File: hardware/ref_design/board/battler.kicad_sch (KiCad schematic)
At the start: 9 parts

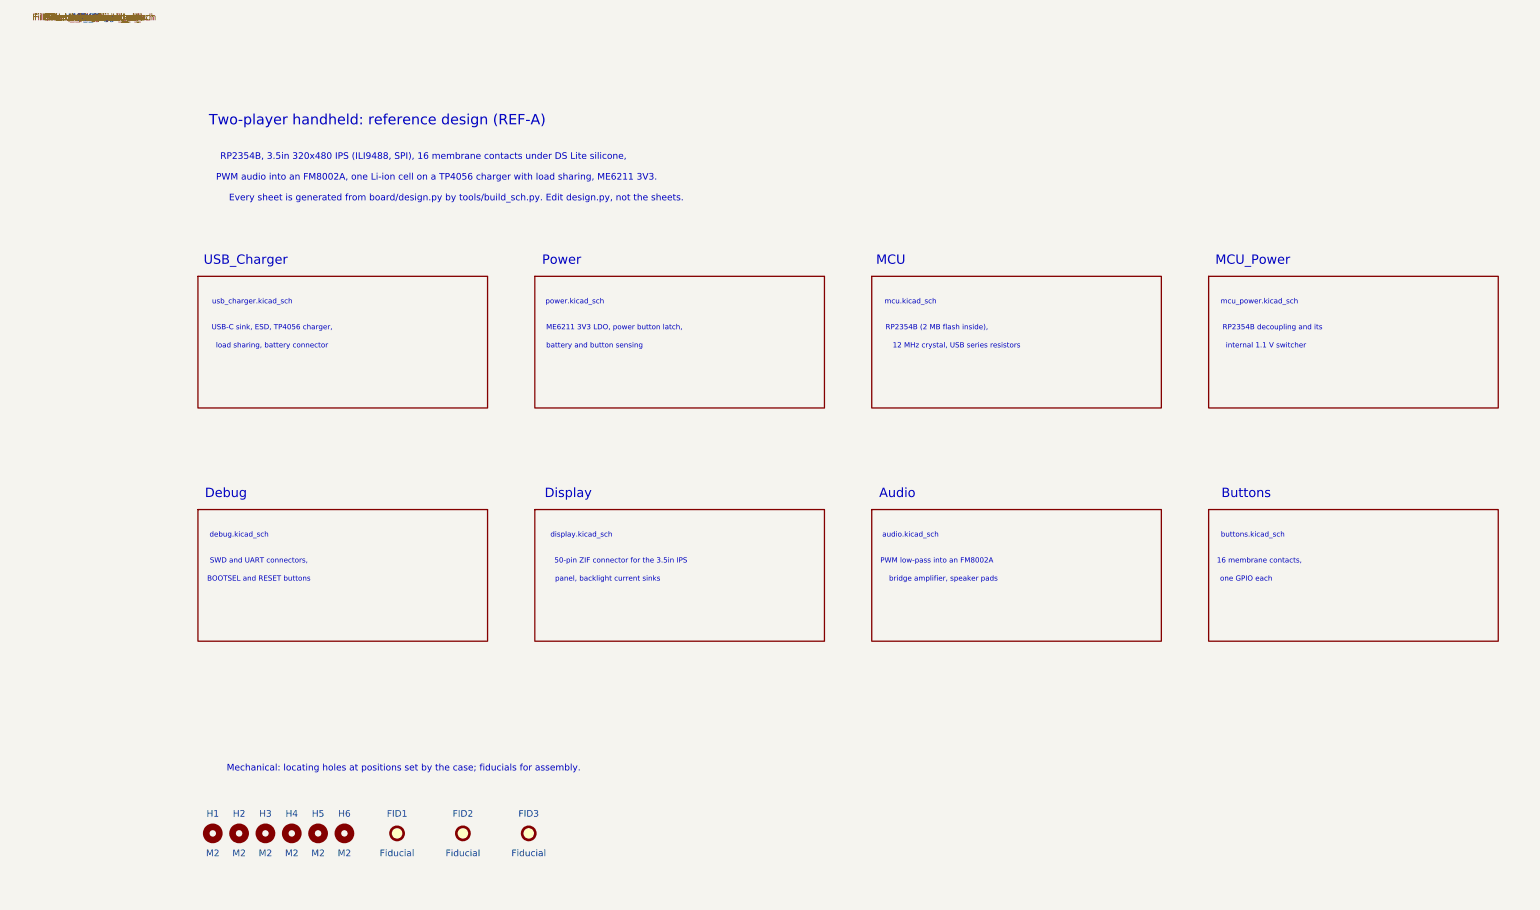
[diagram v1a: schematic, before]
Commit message: Reference schematic: every net named as design.py names it, root sheet notes list each sheet's blocks, measured font widths, and Konnect notes updated for the new workarounds.
Co-Authored-By: Claude Opus 5.5 <noreply@anthropic.com>
Claude-Session: https://claude.ai/code/session_01NxPKqL46d94oRzrtCbFjri
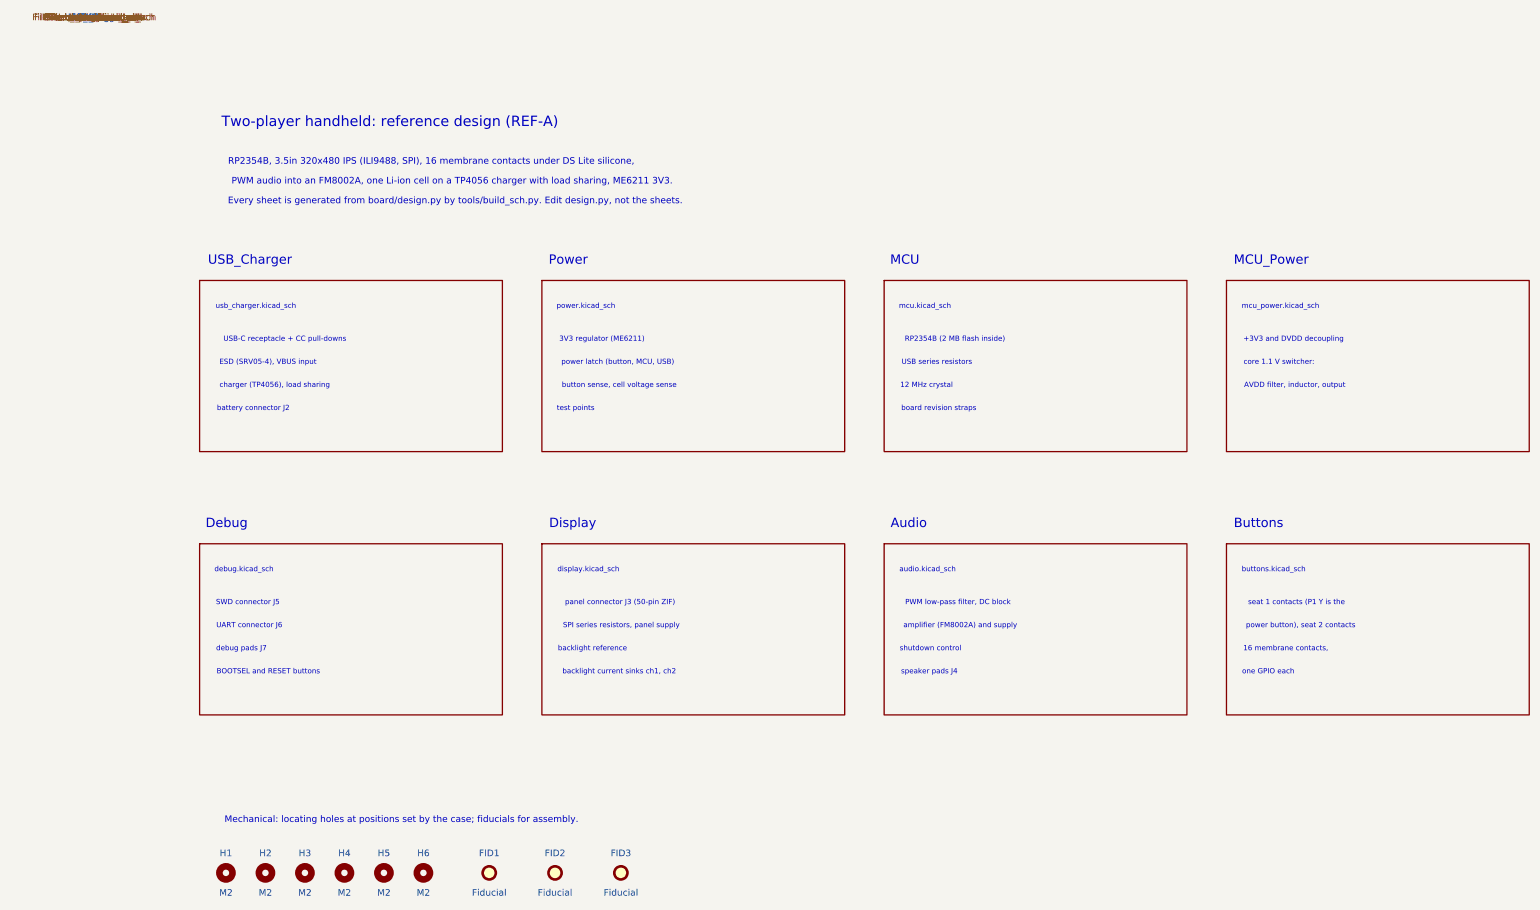
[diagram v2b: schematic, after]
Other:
- note added: "+3V3 and DVDD decoupling"
- note added: "12 MHz crystal"
- note added: "3V3 regulator (ME6211)"
- note added: "AVDD filter, inductor, output"
- note added: "ESD (SRV05-4), VBUS input"
- note added: "PWM low-pass filter, DC block"
- note added: "RP2354B (2 MB flash inside)"
- note added: "SPI series resistors, panel supply"
- note added: "SWD connector J5"
- note added: "UART connector J6"
- note added: "USB series resistors"
- note added: "USB-C receptacle + CC pull-downs"
- note added: "amplifier (FM8002A) and supply"
- note added: "backlight current sinks ch1, ch2"
- note added: "backlight reference"
- note added: "battery connector J2"
- note added: "board revision straps"
- note added: "button sense, cell voltage sense"
- note added: "charger (TP4056), load sharing"
- note added: "core 1.1 V switcher:"
- note added: "debug pads J7"
- note added: "panel connector J3 (50-pin ZIF)"
- note added: "power button), seat 2 contacts"
- note added: "power latch (button, MCU, USB)"
- note added: "seat 1 contacts (P1 Y is the"
- note added: "shutdown control"
- note added: "speaker pads J4"
- note added: "test points"
- note removed: "12 MHz crystal, USB series resistors"
- note removed: "50-pin ZIF connector for the 3.5in IPS"
- note removed: "ME6211 3V3 LDO, power button latch,"
- note removed: "PWM low-pass into an FM8002A"
- note removed: "RP2354B (2 MB flash inside),"
- note removed: "RP2354B decoupling and its"
- note removed: "SWD and UART connectors,"
- note removed: "USB-C sink, ESD, TP4056 charger,"
- note removed: "battery and button sensing"
- note removed: "bridge amplifier, speaker pads"
- note removed: "internal 1.1 V switcher"
- note removed: "load sharing, battery connector"
- note removed: "panel, backlight current sinks"

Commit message: Reference schematic: Start and Select blocks per seat on the Buttons sheet, P1 Start drawn on the power path, notes name Start as the power button.
Co-Authored-By: Claude Opus 5.5 <noreply@anthropic.com>
Claude-Session: https://claude.ai/code/session_01NxPKqL46d94oRzrtCbFjri
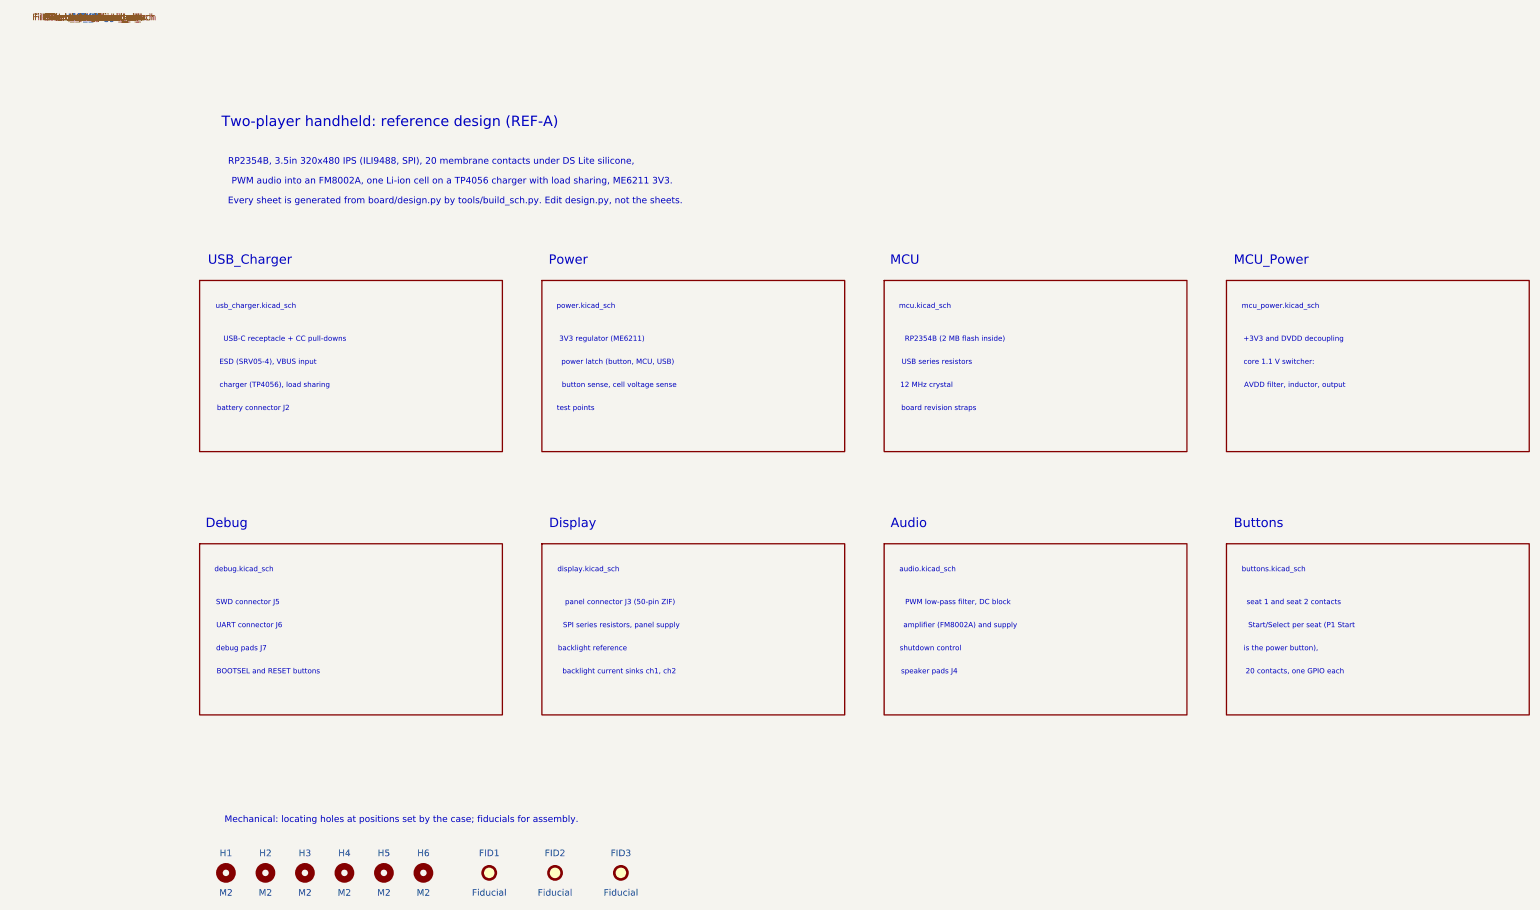
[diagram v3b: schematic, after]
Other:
- note added: "20 contacts, one GPIO each"
- note added: "RP2354B, 3.5in 320x480 IPS (ILI9488, SPI), 20 membrane contacts under DS Lite silicone,"
- note added: "Start/Select per seat (P1 Start"
- note added: "is the power button),"
- note added: "seat 1 and seat 2 contacts"
- note removed: "16 membrane contacts,"
- note removed: "RP2354B, 3.5in 320x480 IPS (ILI9488, SPI), 16 membrane contacts under DS Lite silicone,"
- note removed: "one GPIO each"
- note removed: "power button), seat 2 contacts"
- note removed: "seat 1 contacts (P1 Y is the"
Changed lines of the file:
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@@
     (effects (font (size 2 2)))
   )
-  (text "RP2354B, 3.5in 320x480 IPS (ILI9488, SPI), 16 membrane contacts under DS Lite silicone,"
+  (text "RP2354B, 3.5in 320x480 IPS (ILI9488, SPI), 20 membrane contacts under DS Lite silicone,"
     (at 65.008 27.94 0)
     (effects (font (size 1.27 1.27)))
@@
     (effects (font (size 1 1)))
   )
-  (text "seat 1 contacts (P1 Y is the"
-    (at 231.956 113.03 0)
-    (effects (font (size 1 1)))
-  )
-  (text "power button), seat 2 contacts"
-    (at 232.766 117.48 0)
-    (effects (font (size 1 1)))
-  )
-  (text "16 membrane contacts,"
-    (at 229.885 121.93 0)
-    (effects (font (size 1 1)))
-  )
-  (text "one GPIO each"
-    (at 226.504 126.38 0)
-    (effects (font (size 1 1)))
-  )
+  (text "seat 1 and seat 2 contacts"
+    (at 231.433 113.03 0)
+    (effects (font (size 1 1)))
+  )
+  (text "Start/Select per seat (P1 Start"
+    (at 232.931 117.48 0)
+    (effects (font (size 1 1)))
+  )
+  (text "is the power button),"
+    (at 228.957 121.93 0)
+    (effects (font (size 1 1)))
+  )
+  (text "20 contacts, one GPIO each"
+    (at 231.647 126.38 0)
+    (effects (font (size 1 1)))
+  )

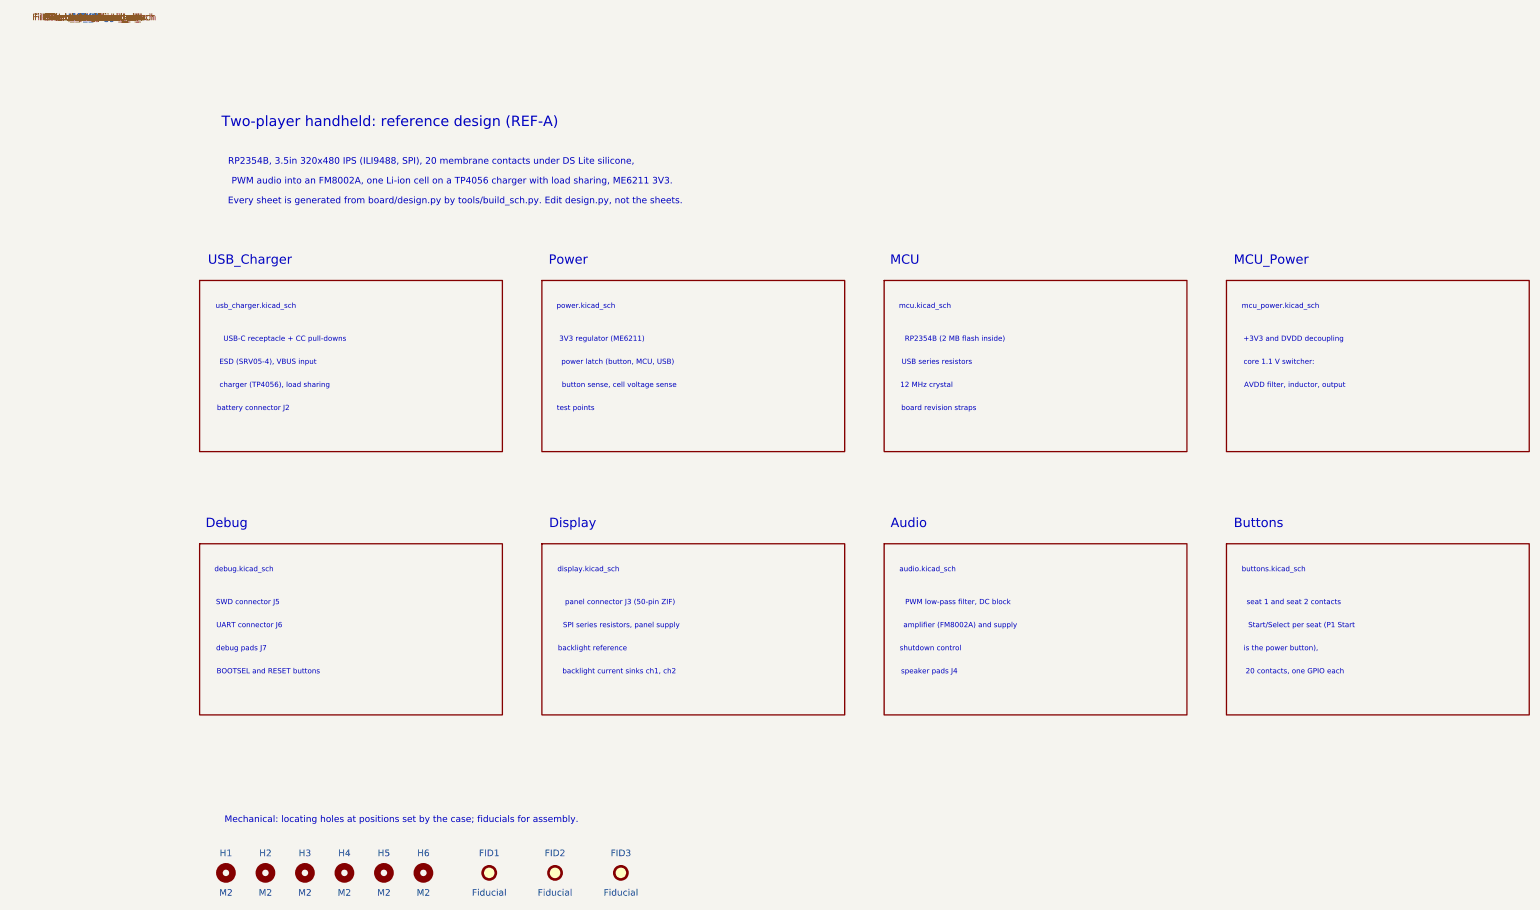
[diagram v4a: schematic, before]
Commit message: Reference schematic: written directly in KiCad 10's format and cleaned up sheet by sheet
tools/schwrite.py writes each sheet whole (library symbols flattened as KiCad caches
them, stable UUIDs, round-trip checked against KiCad's writer) instead of Konnect,
which couldn't hide a power symbol's #PWR reference or place a field: those were the
fields parked at every page's top-left. Power rails are KiCad's own symbols showing
their name; the transistors and the MCU use their real KiCad symbols; global labels
point the way their wire runs. Sheets: U3's CE wired to the latch, the ESD array on
D+/D-, the USB resistors and crystal wired to the RP2354B, J7's BOOTSEL pad wired to
its button, TP7/TP8 moved onto their nets' sheets, the FM8002A symbol widened so its
pin names clear. ERC 0, netlist check PASS (same parts, values, footprints and
connectivity; LS_GATE and AMP_SHDN are now sheet-local).

tools/sync_pcb.py brings the routed board in line without re-routing (symbol links,
fields, the two renamed nets, no-connect pads on their unconnected-(...) nets, which
KiCad's parity check expects); build_pcb.py gives no-connect pads the same nets
(copper unchanged). check_pcb PASS: 0 unconnected, 0 parity issues.

Co-Authored-By: Claude Opus 5.5 <noreply@anthropic.com>
Claude-Session: https://claude.ai/code/session_01Y3mFMxLYqNeyyedvbYuRwX
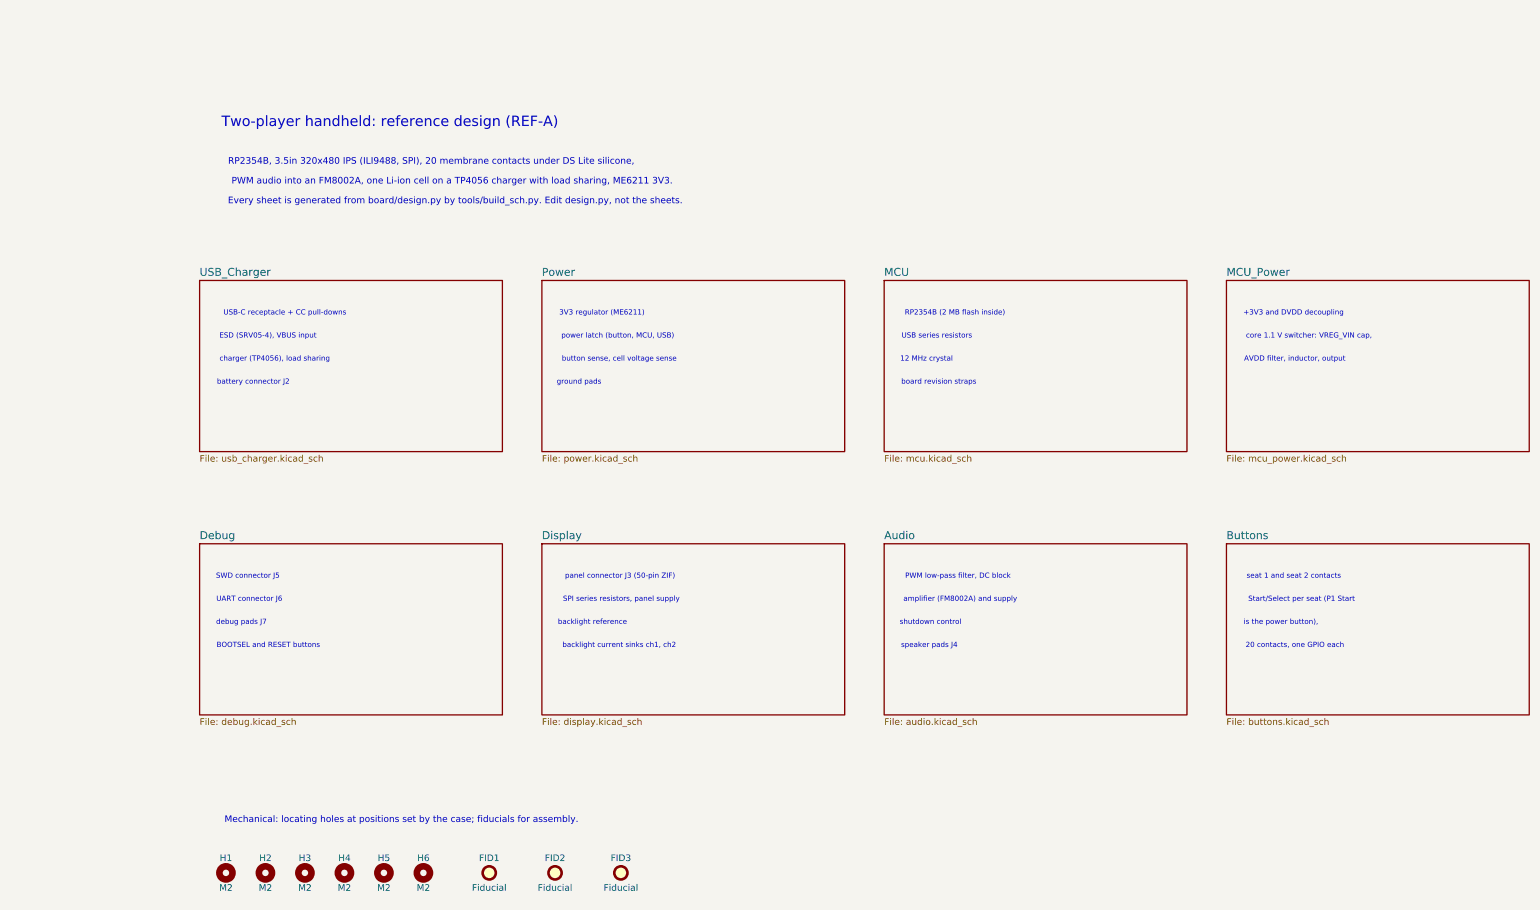
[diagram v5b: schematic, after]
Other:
- note added: "core 1.1 V switcher: VREG_VIN cap,"
- note added: "ground pads"
- note removed: "Audio"
- note removed: "Buttons"
- note removed: "Debug"
- note removed: "Display"
- note removed: "MCU"
- note removed: "MCU_Power"
- note removed: "Power"
- note removed: "USB_Charger"
- note removed: "audio.kicad_sch"
- note removed: "buttons.kicad_sch"
- note removed: "core 1.1 V switcher:"
- note removed: "debug.kicad_sch"
- note removed: "display.kicad_sch"
- note removed: "mcu.kicad_sch"
- note removed: "mcu_power.kicad_sch"
- note removed: "power.kicad_sch"
- note removed: "test points"
- note removed: "usb_charger.kicad_sch"
- company: (none) -> Two-player handheld: reference design (REF-A)
- title: (none) -> Sheets and mechanical parts
